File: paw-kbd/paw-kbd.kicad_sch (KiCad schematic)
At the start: 46 parts, among them J1 OLED, J2 MJ-4PP-9, SW1 SW_PUSH, SW10 SW_PUSH, SW11 SW_PUSH, SW12 SW_PUSH, SW13 SW_PUSH, SW14 SW_PUSH, SW15 SW_PUSH, SW16 SW_PUSH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

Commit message: optional socketed footprints
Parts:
- SW1, SW10, SW11, SW12, SW13, SW14, SW15, SW2, SW3, SW4, SW5, SW6, SW7, SW8, SW9: footprint keeb-footprints:ChocV1_V2_Hotswap_reversed_choc_spacing -> keeb-footprints:ChocV1_V2_Hotswap_optional_reversed_choc_spacing
- SW16: footprint keeb-footprints:ChocV1_V2_Hotswap_reversed_choc_spacing -> keeb-footprints:ChocV1_V2_Hotswap_optional_reversed_15u_choc_spacing
- SW17: footprint keeb-footprints:ChocV1_V2_Hotswap_reversed_15u_choc_spacing -> keeb-footprints:ChocV1_V2_Hotswap_optional_reversed_15u_choc_spacing

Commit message: oval outline
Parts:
- D1, D10, D11, D12, D13, D14, D15, D16, D17, D2, D3, D4, D5, D6, D7, D8, D9: footprint keeb-footprints:D3_SMD -> kbd:D3_TH_SMD_v2
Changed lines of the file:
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@@
       (effects (font (size 1.27 1.27)) (justify left) hide)
     )
-    (property "Footprint" "keeb-footprints:D3_SMD" (id 2) (at 182.88 57.785 0)
+    (property "Footprint" "kbd:D3_TH_SMD_v2" (id 2) (at 182.88 57.785 0)
       (effects (font (size 1.27 1.27)) hide)
     )
@@
       (effects (font (size 1.27 1.27)) (justify left) hide)
     )
-    (property "Footprint" "keeb-footprints:D3_SMD" (id 2) (at 161.925 45.72 0)
+    (property "Footprint" "kbd:D3_TH_SMD_v2" (id 2) (at 161.925 45.72 0)
       (effects (font (size 1.27 1.27)) hide)
     )
@@
       (effects (font (size 1.27 1.27)) (justify left) hide)
     )
-    (property "Footprint" "keeb-footprints:D3_SMD" (id 2) (at 204.47 57.785 0)
+    (property "Footprint" "kbd:D3_TH_SMD_v2" (id 2) (at 204.47 57.785 0)
       (effects (font (size 1.27 1.27)) hide)
     )
@@
       (effects (font (size 1.27 1.27)) (justify left) hide)
     )
-    (property "Footprint" "keeb-footprints:D3_SMD" (id 2) (at 204.47 69.85 0)
+    (property "Footprint" "kbd:D3_TH_SMD_v2" (id 2) (at 204.47 69.85 0)
       (effects (font (size 1.27 1.27)) hide)
     )
@@
       (effects (font (size 1.27 1.27)) (justify left) hide)
     )
-    (property "Footprint" "keeb-footprints:D3_SMD" (id 2) (at 182.88 45.72 0)
+    (property "Footprint" "kbd:D3_TH_SMD_v2" (id 2) (at 182.88 45.72 0)
       (effects (font (size 1.27 1.27)) hide)
     )
@@
       (effects (font (size 1.27 1.27)) (justify left) hide)
     )
-    (property "Footprint" "keeb-footprints:D3_SMD" (id 2) (at 161.925 57.785 0)
+    (property "Footprint" "kbd:D3_TH_SMD_v2" (id 2) (at 161.925 57.785 0)
       (effects (font (size 1.27 1.27)) hide)
     )
@@
       (effects (font (size 1.27 1.27)) (justify left) hide)
     )
-    (property "Footprint" "keeb-footprints:D3_SMD" (id 2) (at 248.92 81.915 0)
+    (property "Footprint" "kbd:D3_TH_SMD_v2" (id 2) (at 248.92 81.915 0)
       (effects (font (size 1.27 1.27)) hide)
     )
@@
       (effects (font (size 1.27 1.27)) (justify left) hide)
     )
-    (property "Footprint" "keeb-footprints:D3_SMD" (id 2) (at 226.695 45.72 0)
+    (property "Footprint" "kbd:D3_TH_SMD_v2" (id 2) (at 226.695 45.72 0)
       (effects (font (size 1.27 1.27)) hide)
     )
@@
       (effects (font (size 1.27 1.27)) (justify left) hide)
     )
-    (property "Footprint" "keeb-footprints:D3_SMD" (id 2) (at 182.88 69.85 0)
+    (property "Footprint" "kbd:D3_TH_SMD_v2" (id 2) (at 182.88 69.85 0)
       (effects (font (size 1.27 1.27)) hide)
     )
@@
       (effects (font (size 1.27 1.27)) (justify left) hide)
     )
-    (property "Footprint" "keeb-footprints:D3_SMD" (id 2) (at 204.47 45.72 0)
+    (property "Footprint" "kbd:D3_TH_SMD_v2" (id 2) (at 204.47 45.72 0)
       (effects (font (size 1.27 1.27)) hide)
     )
@@
       (effects (font (size 1.27 1.27)) (justify left) hide)
     )
-    (property "Footprint" "keeb-footprints:D3_SMD" (id 2) (at 248.92 57.785 0)
+    (property "Footprint" "kbd:D3_TH_SMD_v2" (id 2) (at 248.92 57.785 0)
       (effects (font (size 1.27 1.27)) hide)
     )
@@
       (effects (font (size 1.27 1.27)) (justify left) hide)
     )
-    (property "Footprint" "keeb-footprints:D3_SMD" (id 2) (at 248.92 69.85 0)
+    (property "Footprint" "kbd:D3_TH_SMD_v2" (id 2) (at 248.92 69.85 0)
       (effects (font (size 1.27 1.27)) hide)
     )
@@
       (effects (font (size 1.27 1.27)) (justify left) hide)
     )
-    (property "Footprint" "keeb-footprints:D3_SMD" (id 2) (at 226.695 57.785 0)
+    (property "Footprint" "kbd:D3_TH_SMD_v2" (id 2) (at 226.695 57.785 0)
       (effects (font (size 1.27 1.27)) hide)
     )
@@
       (effects (font (size 1.27 1.27)) (justify left) hide)
     )
-    (property "Footprint" "keeb-footprints:D3_SMD" (id 2) (at 226.695 69.85 0)
+    (property "Footprint" "kbd:D3_TH_SMD_v2" (id 2) (at 226.695 69.85 0)
       (effects (font (size 1.27 1.27)) hide)
     )
@@
       (effects (font (size 1.27 1.27)) (justify left) hide)
     )
-    (property "Footprint" "keeb-footprints:D3_SMD" (id 2) (at 161.925 69.85 0)
+    (property "Footprint" "kbd:D3_TH_SMD_v2" (id 2) (at 161.925 69.85 0)
       (effects (font (size 1.27 1.27)) hide)
     )
@@
       (effects (font (size 1.27 1.27)) (justify left) hide)
     )
-    (property "Footprint" "keeb-footprints:D3_SMD" (id 2) (at 248.92 45.72 0)
+    (property "Footprint" "kbd:D3_TH_SMD_v2" (id 2) (at 248.92 45.72 0)
       (effects (font (size 1.27 1.27)) hide)
     )
@@
       (effects (font (size 1.27 1.27)) (justify left) hide)
     )
-    (property "Footprint" "keeb-footprints:D3_SMD" (id 2) (at 226.695 81.915 0)
+    (property "Footprint" "kbd:D3_TH_SMD_v2" (id 2) (at 226.695 81.915 0)
       (effects (font (size 1.27 1.27)) hide)
     )
@@
     )
     (path "/0b9ccb6b-48e0-4f25-a0e2-b85efb27414d"
-      (reference "D1") (unit 1) (value "DIODE") (footprint "keeb-footprints:D3_SMD")
+      (reference "D1") (unit 1) (value "DIODE") (footprint "kbd:D3_TH_SMD_v2")
     )
     (path "/20950f5b-b3d1-4a12-9892-fa948fcd077d"
-      (reference "D2") (unit 1) (value "DIODE") (footprint "keeb-footprints:D3_SMD")
+      (reference "D2") (unit 1) (value "DIODE") (footprint "kbd:D3_TH_SMD_v2")
     )
     (path "/92ee02f0-b223-42ef-a597-116e1d1f5d16"
-      (reference "D3") (unit 1) (value "DIODE") (footprint "keeb-footprints:D3_SMD")
+      (reference "D3") (unit 1) (value "DIODE") (footprint "kbd:D3_TH_SMD_v2")
     )
     (path "/1f21a49b-0be6-462a-898f-9d4c5bc8446e"
-      (reference "D4") (unit 1) (value "DIODE") (footprint "keeb-footprints:D3_SMD")
+      (reference "D4") (unit 1) (value "DIODE") (footprint "kbd:D3_TH_SMD_v2")
     )
     (path "/03729957-b9ab-4bcf-abb9-f816f2e7aa69"
-      (reference "D5") (unit 1) (value "DIODE") (footprint "keeb-footprints:D3_SMD")
+      (reference "D5") (unit 1) (value "DIODE") (footprint "kbd:D3_TH_SMD_v2")
     )
     (path "/4ed8cc87-36a2-4496-9d5f-087e44730bf7"
-      (reference "D6") (unit 1) (value "DIODE") (footprint "keeb-footprints:D3_SMD")
+      (reference "D6") (unit 1) (value "DIODE") (footprint "kbd:D3_TH_SMD_v2")
     )
     (path "/560229e7-b47d-4701-ab20-50bdc7bf7451"
-      (reference "D7") (unit 1) (value "DIODE") (footprint "keeb-footprints:D3_SMD")
+      (reference "D7") (unit 1) (value "DIODE") (footprint "kbd:D3_TH_SMD_v2")
     )
     (path "/0eaf2e5b-c61f-44ec-90ae-fb79af0c5219"
-      (reference "D8") (unit 1) (value "DIODE") (footprint "keeb-footprints:D3_SMD")
+      (reference "D8") (unit 1) (value "DIODE") (footprint "kbd:D3_TH_SMD_v2")
     )
     (path "/10726248-85c0-4c87-8a22-07c68f33d07a"
-      (reference "D9") (unit 1) (value "DIODE") (footprint "keeb-footprints:D3_SMD")
+      (reference "D9") (unit 1) (value "DIODE") (footprint "kbd:D3_TH_SMD_v2")
     )
     (path "/39898631-7ba9-4594-a2e0-a563839b0874"
-      (reference "D10") (unit 1) (value "DIODE") (footprint "keeb-footprints:D3_SMD")
+      (reference "D10") (unit 1) (value "DIODE") (footprint "kbd:D3_TH_SMD_v2")
     )
     (path "/726a7d31-b89a-4678-9864-93dc8c96091b"
-      (reference "D11") (unit 1) (value "DIODE") (footprint "keeb-footprints:D3_SMD")
+      (reference "D11") (unit 1) (value "DIODE") (footprint "kbd:D3_TH_SMD_v2")
     )
     (path "/88a3836e-f244-4c08-9052-8a381e2c7349"
-      (reference "D12") (unit 1) (value "DIODE") (footprint "keeb-footprints:D3_SMD")
+      (reference "D12") (unit 1) (value "DIODE") (footprint "kbd:D3_TH_SMD_v2")
     )
     (path "/f1dfdc0b-a202-43ee-9eef-9c9c74472572"
-      (reference "D13") (unit 1) (value "DIODE") (footprint "keeb-footprints:D3_SMD")
+      (reference "D13") (unit 1) (value "DIODE") (footprint "kbd:D3_TH_SMD_v2")
     )
     (path "/576ebb09-3d71-4624-b818-657f1ac927a9"
-      (reference "D14") (unit 1) (value "DIODE") (footprint "keeb-footprints:D3_SMD")
+      (reference "D14") (unit 1) (value "DIODE") (footprint "kbd:D3_TH_SMD_v2")
     )
     (path "/656804e7-18c2-4ed0-bafb-02254d000861"
-      (reference "D15") (unit 1) (value "DIODE") (footprint "keeb-footprints:D3_SMD")
+      (reference "D15") (unit 1) (value "DIODE") (footprint "kbd:D3_TH_SMD_v2")
     )
     (path "/f27dab61-da24-4169-8399-d7692b7e95e0"
-      (reference "D16") (unit 1) (value "DIODE") (footprint "keeb-footprints:D3_SMD")
+      (reference "D16") (unit 1) (value "DIODE") (footprint "kbd:D3_TH_SMD_v2")
     )
     (path "/2e8e89dd-4e1f-499c-8581-424796456d63"
-      (reference "D17") (unit 1) (value "DIODE") (footprint "keeb-footprints:D3_SMD")
+      (reference "D17") (unit 1) (value "DIODE") (footprint "kbd:D3_TH_SMD_v2")
     )
     (path "/ce046486-0921-4e3c-9d22-c9a24f07937b"

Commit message: wip
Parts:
- added J3: TRACKBALL, keeb-footprints:pimoroni, symbol Connector_Generic:Conn_01x05
- added JP10, JP11, JP12, JP14, JP9: Device_Jumper_NO_Small, kbd:Jumper, symbol KLORlib:Device_Jumper_NO_Small
- added JP13: Device_Jumper_NO_Small, kbd:Jumper, symbol SofleKeyboard-cache:Device_Jumper_NO_Small
- added SW18: RotaryEncoder_Switch, Rotary_Encoder:RotaryEncoder_Alps_EC12E-Switch_Vertical_H20mm, symbol Device:RotaryEncoder_Switch
- J1: footprint kbd:OLED_v2 -> keeb-footprints:SSD1306_128x64OLED
- U1: footprint keeb-footprints:ProMicro_unrouted_type_c -> keeb-footprints:ProMicro_v2
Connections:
- net GND: now also JP11.2, JP12.2, SW18.C
- net SCL: now also JP10.2, JP13.2
- net SDA: now also JP14.2, JP9.2
- net VCC: now also J3.3 (Pin_3)
- new net: J3.2 (Pin_2), JP10.1, JP12.1
- new net: J3.1 (Pin_1), JP9.1
- new net: J3.4 (Pin_4), JP11.1, JP13.1
- new net: J3.5 (Pin_5), JP14.1
- new net ENCA: SW18.A
- new net ENCB: SW18.B
- new net SW18A: SW18.S1
- new net SW18B: SW18.S2
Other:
- note added: "ENCODER"
- note added: "TRACKBALL MODULE"

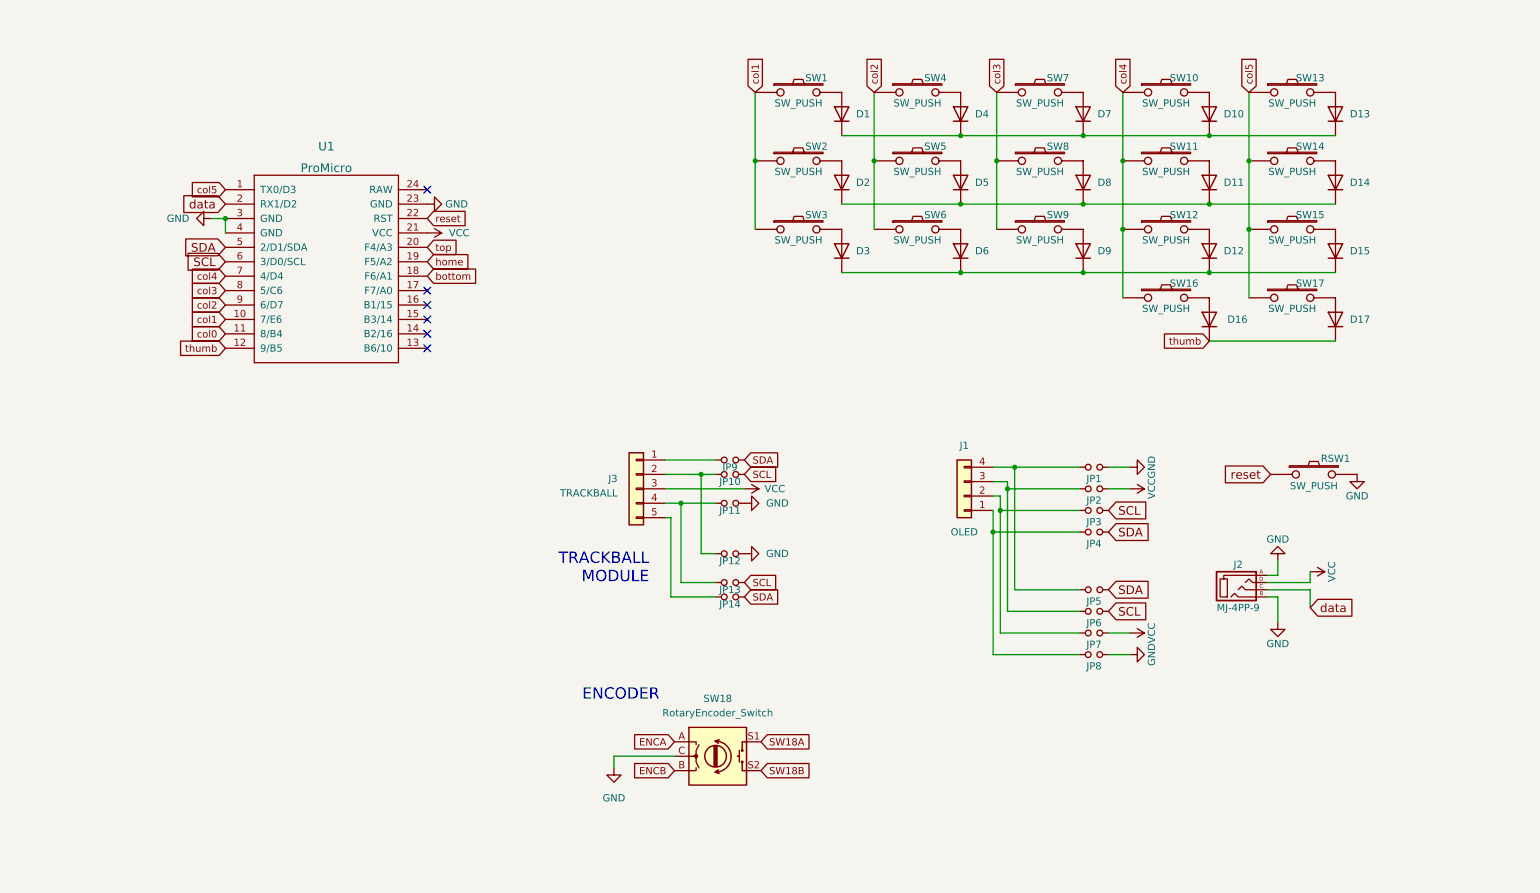
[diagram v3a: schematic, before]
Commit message: big oled
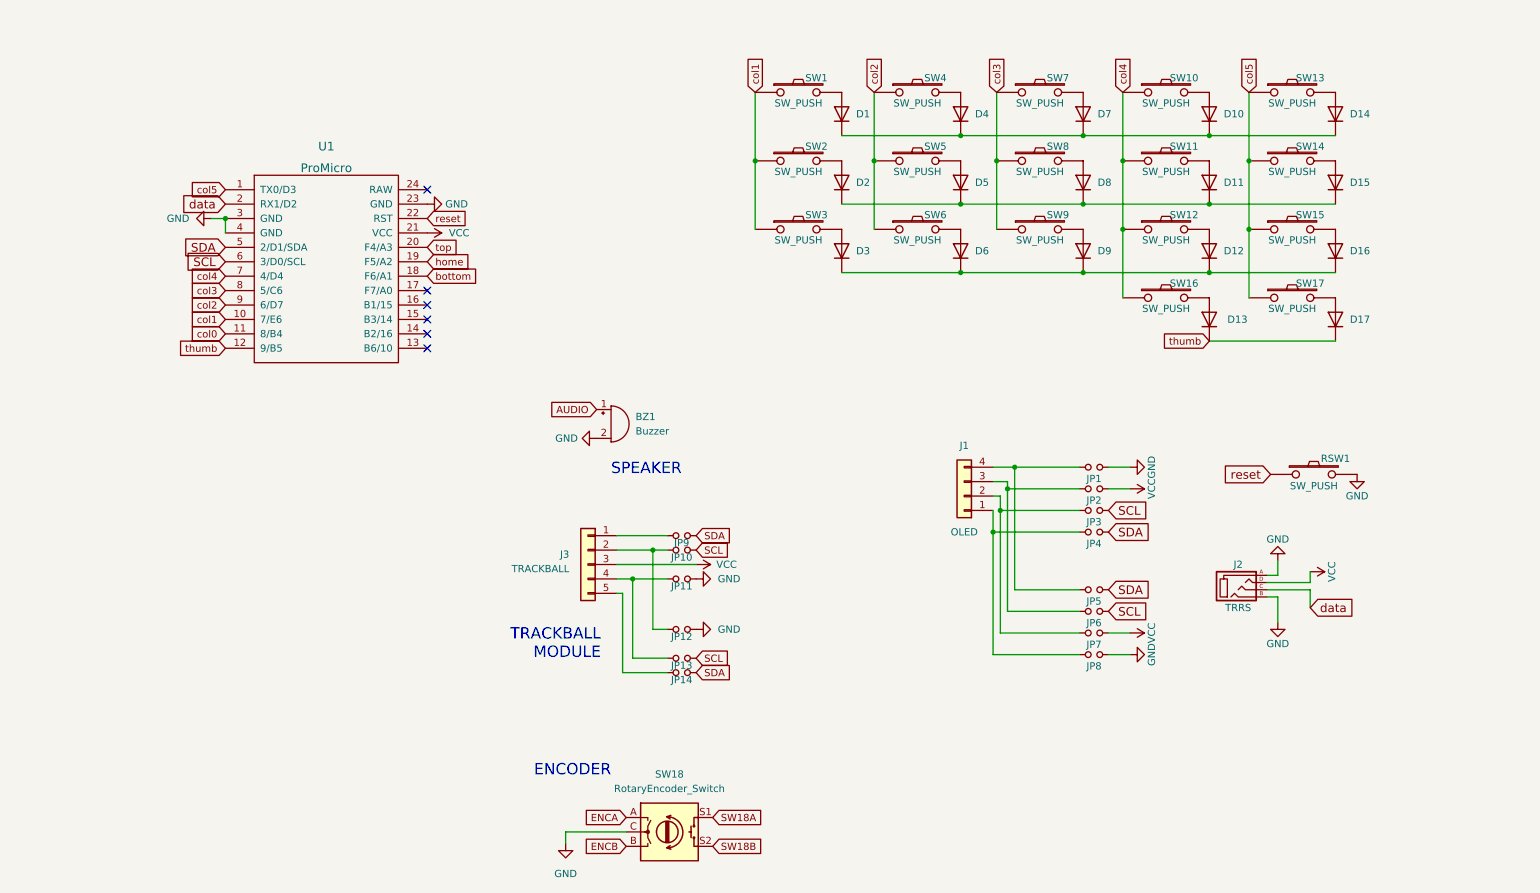
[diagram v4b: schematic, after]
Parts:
- added BZ1: Buzzer, Buzzer_Beeper:Buzzer_Mallory_AST1109MLTRQ, symbol Device:Buzzer
- J2: value MJ-4PP-9 -> TRRS
- renumbered D16 to D13, D13 to D14, D14 to D15, D15 to D16
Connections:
- net GND: now also BZ1.2 (+)
- new net AUDIO: BZ1.1 (-)
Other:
- note added: "SPEAKER"
- moved on the sheet: J3, JP10, JP11, JP12, JP13, JP14, JP9, SW18

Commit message: pimoroni trackball footprint
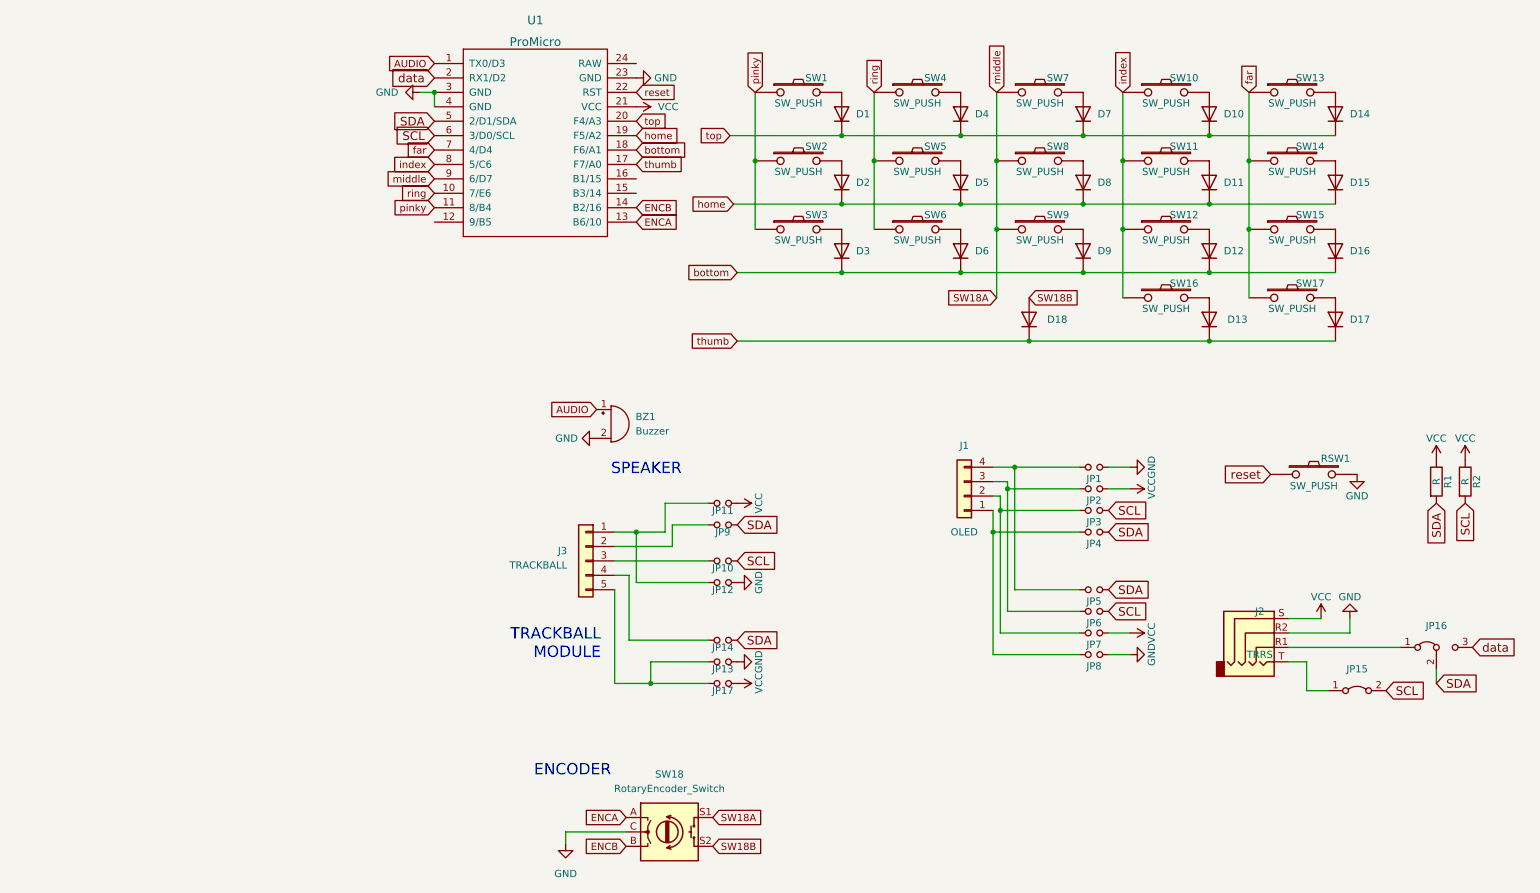
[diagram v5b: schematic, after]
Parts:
- removed JP13: Device_Jumper_NO_Small, kbd:Jumper, symbol SofleKeyboard-cache:Device_Jumper_NO_Small
- added D18: DIODE, kbd:D3_TH_SMD_v2, symbol Simulation_SPICE:DIODE
- added JP13, JP17: Device_Jumper_NO_Small, kbd:Jumper, symbol KLORlib:Device_Jumper_NO_Small
- added JP15: Jumper_2_Bridged, Jumper:SolderJumper-2_P1.3mm_Bridged_Pad1.0x1.5mm, symbol Jumper:Jumper_2_Bridged
- added JP16: Jumper_3_Bridged12, Jumper:SolderJumper-3_P1.3mm_Bridged12_Pad1.0x1.5mm, symbol Jumper:Jumper_3_Bridged12
- added R1, R2: R, kbd:R, symbol Device:R
- J2: symbol corne-chocolate-rescue:MJ-4PP-9-kbd -> Connector:AudioJack4
- J3: footprint keeb-footprints:pimoroni -> keeb-footprints:pimoroni_trackball
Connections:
- net AUDIO: now also U1.1 (TX0/D3)
- net ENCA: now also U1.13 (B6/10)
- net ENCB: now also U1.14 (B2/16)
- net GND: now also J2.R2, JP13.2; no longer J2.A, J2.B, JP11.2
- net SCL: now also JP15.2 (B), R2.2
- net SDA: now also JP16.2 (C), R1.2
- net SW18A: now also SW7.1, SW8.1, SW9.1, U1.9 (6/D7)
- net SW18B: now also D18.1 (A)
- net VCC: now also J2.S, JP11.2, JP17.2, R1.1, R2.1; no longer J2.D, J3.3 (Pin_3)
- net bottom: now also D12.2 (K), D16.2 (K), D3.2 (K), D6.2 (K), D9.2 (K)
- net data: now also JP16.3 (B); no longer J2.C
- net home: now also D11.2 (K), D15.2 (K), D2.2 (K), D5.2 (K), D8.2 (K)
- net thumb: now also U1.17 (F7/A0), D18.2 (K); no longer U1.12 (9/B5)
- net top: now also D1.2 (K), D10.2 (K), D14.2 (K), D4.2 (K), D7.2 (K)
- net at J3.1 (Pin_1): now also JP11.1, JP12.1; no longer JP9.1
- net at J3.4 (Pin_4): now also JP14.1; no longer JP11.1
- net at J3.5 (Pin_5): now also JP13.1, JP17.1; no longer JP14.1
- net col0 renamed pinky
- net pinky: now also SW1.1, SW2.1, SW3.1
- removed net col1: SW1.1, SW2.1, SW3.1, U1.10 (7/E6)
- net col2 renamed ring
- net ring: now also U1.10 (7/E6); no longer U1.9 (6/D7)
- removed net col3: SW7.1, SW8.1, SW9.1, U1.8 (5/C6)
- net col4 renamed index
- net index: now also U1.8 (5/C6); no longer U1.7 (4/D4)
- net col5 renamed far
- net far: now also U1.7 (4/D4); no longer U1.1 (TX0/D3)
- new net: J2.T, JP15.1 (A)
- new net: J2.R1, JP16.1 (A)
- new net: J3.2 (Pin_2), JP9.1
- new net: J3.3 (Pin_3), JP10.1
- no-connect marks 6 -> 0
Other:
- moved on the sheet: J3, JP11, U1

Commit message: 2023-07-29 15:25:01
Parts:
- added SW18: SW_PUSH, keeb-footprints:ChocV1_V2_Hotswap_optional_reversed_choc_spacing, symbol kbd:SW_PUSH
- D1, D10, D11, D12, D13, D14, D15, D16, D17, D18, D2, D3, D4, D5, D6, D7, D8, D9: value DIODE -> ${SIM.PARAMS}; Spice_Netlist_Enabled Y -> (none); Spice_Primitive D -> (none)
- SW16, SW17: footprint keeb-footprints:ChocV1_V2_Hotswap_optional_reversed_15u_choc_spacing -> keeb-footprints:ChocV1_V2_Hotswap_optional_reversed_choc_spacing
- renumbered SW18 to SW19
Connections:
- net far: now also SW18.1; no longer SW17.1
- net index: now also SW17.1; no longer SW16.1
- net SW18A renamed middle
- net middle: now also SW16.1; no longer SW19.S1
- net SW18B: no longer names the net of D18.1 (A)
- net SW18B: now also SW18.2; no longer SW19.S2
- new net SW19A: SW19.S1
- new net SW19B: SW19.S2
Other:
- moved on the sheet: D13, D17, SW16, SW17
